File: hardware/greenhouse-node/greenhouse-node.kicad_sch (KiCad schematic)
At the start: 53 parts, among them J1 Conn_01x12_Male, J2 Conn_01x02_Male, J3 Conn_01x02_Male, J4 Conn_01x02_Male, J5 Conn_01x04_Male, J7 Conn_01x02_Male, Q1 BC549C, Q2 BC549C, Q3 IRF9530N, Q4 IRF530N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

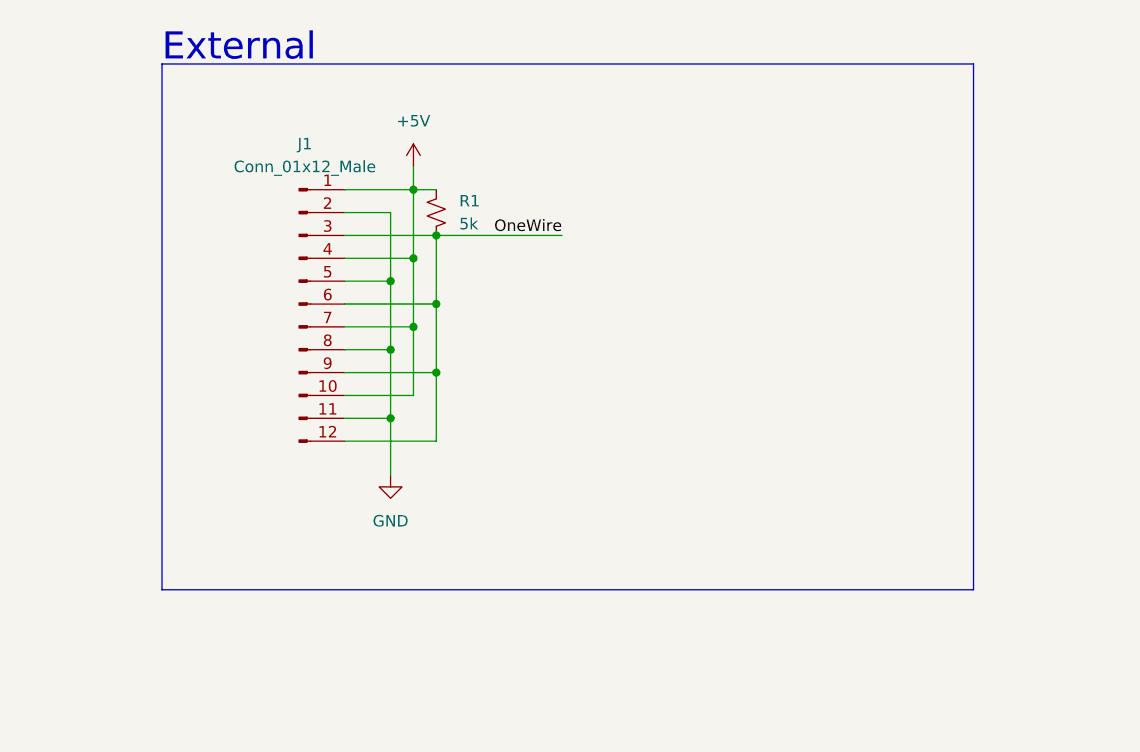
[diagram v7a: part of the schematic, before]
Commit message: Implement HC-12 on node
Also removed switch logic and old shift register
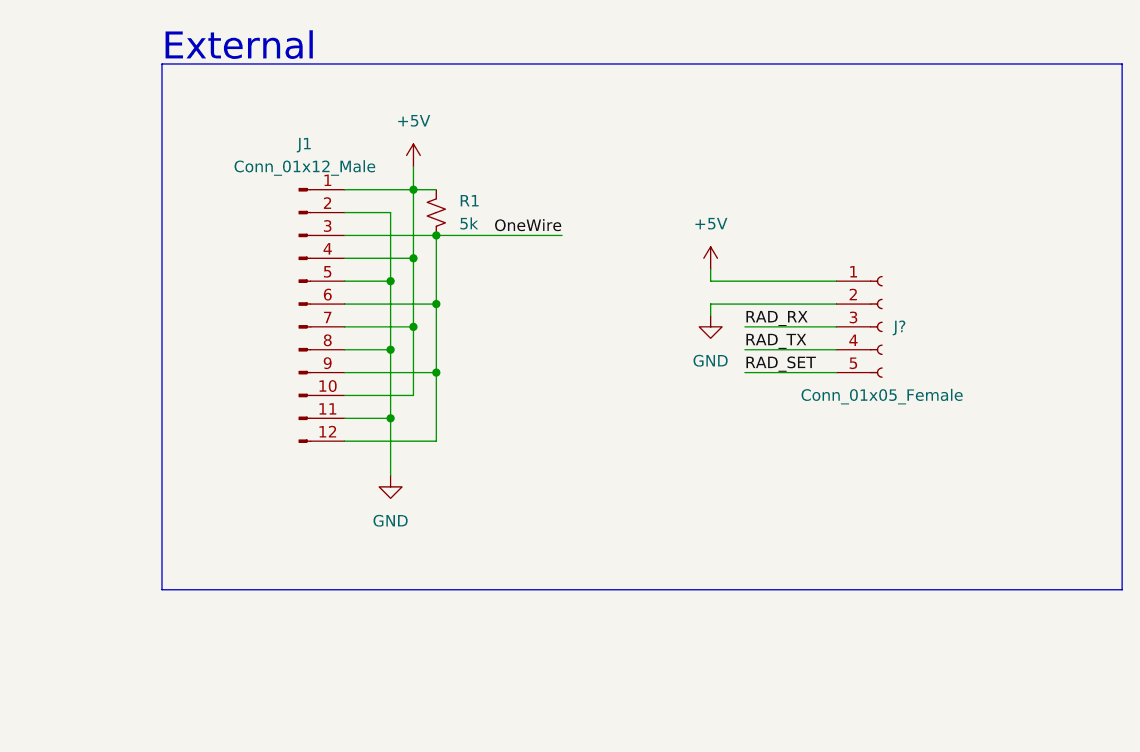
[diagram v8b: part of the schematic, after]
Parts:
- added J?: Conn_01x05_Female, Connector_PinSocket_2.54mm:PinSocket_1x05_P2.54mm_Vertical, symbol Connector:Conn_01x05_Female
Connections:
- net +5V: now also J?.1 (Pin_1)
- net GND: now also J?.2 (Pin_2)
- net RAD_RX: now also J?.3 (Pin_3)
- net RAD_TX: now also J?.4 (Pin_4)
- new net RAD_SET: J?.5 (Pin_5)
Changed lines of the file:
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@@
+    (stroke (width 0) (type default) (color 0 0 0 0))
+  )
+  (wire (pts (xy 281.94 64.77) (xy 292.1 64.77))
     (stroke (width 0) (type default) (color 0 0 0 0))
   )
@@
     (stroke (width 0) (type default) (color 0 0 0 0))
   )
+  (wire (pts (xy 278.13 58.42) (xy 278.13 59.69))
+    (stroke (width 0) (type default) (color 0 0 0 0))
+  )
   (wire (pts (xy 242.57 59.69) (xy 242.57 52.07))
     (stroke (width 0) (type default) (color 0 0 0 0))
@@
     (stroke (width 0) (type default) (color 0 0 0 0))
   )
+  (wire (pts (xy 281.94 69.85) (xy 292.1 69.85))
+    (stroke (width 0) (type default) (color 0 0 0 0))
+  )
   (wire (pts (xy 299.72 213.36) (xy 311.15 213.36))
     (stroke (width 0) (type default) (color 0 0 0 0))
@@
     (stroke (width 0) (type default) (color 0 0 0 0))
   )
+  (wire (pts (xy 278.13 62.23) (xy 278.13 63.5))
+    (stroke (width 0) (type default) (color 0 0 0 0))
+  )
+  (wire (pts (xy 281.94 67.31) (xy 292.1 67.31))
+    (stroke (width 0) (type default) (color 0 0 0 0))
+  )
   (wire (pts (xy 119.38 158.75) (xy 133.35 158.75))
     (stroke (width 0) (type default) (color 0 0 0 0))
@@
     (stroke (width 0) (type default) (color 0 0 0 0))
   )
+  (wire (pts (xy 278.13 59.69) (xy 292.1 59.69))
+    (stroke (width 0) (type default) (color 0 0 0 0))
+  )
   (wire (pts (xy 256.54 166.37) (xy 256.54 163.83))
     (stroke (width 0) (type default) (color 0 0 0 0))
@@
     (stroke (width 0) (type default) (color 0 0 0 0))
   )
-  (polyline (pts (xy 217.17 93.98) (xy 307.34 93.98))
+  (polyline (pts (xy 217.17 93.98) (xy 323.85 93.98))
     (stroke (width 0) (type default) (color 0 0 0 0))
   )
@@
     (stroke (width 0) (type default) (color 0 0 0 0))
   )
+  (wire (pts (xy 292.1 62.23) (xy 278.13 62.23))
+    (stroke (width 0) (type default) (color 0 0 0 0))
+  )
   (wire (pts (xy 149.86 78.74) (xy 152.4 78.74))
     (stroke (width 0) (type default) (color 0 0 0 0))
   )
-  (polyline (pts (xy 307.34 35.56) (xy 217.17 35.56))
+  (polyline (pts (xy 323.85 35.56) (xy 217.17 35.56))
     (stroke (width 0) (type default) (color 0 0 0 0))
   )
@@
     (stroke (width 0) (type default) (color 0 0 0 0))
   )
-  (polyline (pts (xy 307.34 93.98) (xy 307.34 35.56))
+  (polyline (pts (xy 323.85 93.98) (xy 323.85 35.56))
     (stroke (width 0) (type default) (color 0 0 0 0))
   )
@@
     (effects (font (size 1.27 1.27)) (justify right bottom))
   )
+  (label "RAD_TX" (at 281.94 67.31 0)
+    (effects (font (size 1.27 1.27)) (justify left bottom))
+  )
   (label "LED_G" (at 153.67 185.42 0)
     (effects (font (size 1.27 1.27)) (justify left bottom))
@@
     (effects (font (size 1.27 1.27)) (justify right bottom))
   )
+  (label "RAD_RX" (at 281.94 64.77 0)
+    (effects (font (size 1.27 1.27)) (justify left bottom))
+  )
   (label "LED_R" (at 153.67 195.58 0)
     (effects (font (size 1.27 1.27)) (justify left bottom))
@@
   (label "SR_CLK" (at 124.46 227.33 180)
     (effects (font (size 1.27 1.27)) (justify right bottom))
+  )
+  (label "RAD_SET" (at 281.94 69.85 0)
+    (effects (font (size 1.27 1.27)) (justify left bottom))
   )
   (label "XTAL2" (at 125.73 212.09 0)
@@
       (effects (font (size 1.27 1.27)) hide)
     )
+  )
+  (symbol (lib_id "Connector:Conn_01x05_Female") (at 297.18 64.77 0) (unit 1)
+    (in_bom yes) (on_board yes) (fields_autoplaced)
+    (property "Reference" "J?" (id 0) (at 298.45 64.7699 0)
+      (effects (font (size 1.27 1.27)) (justify left))
+    )
+    (property "Value" "Conn_01x05_Female" (id 1) (at 297.18 72.39 0))
+    (property "Footprint" "Connector_PinSocket_2.54mm:PinSocket_1x05_P2.54mm_Vertical" (id 2) (at 297.18 64.77 0)
+      (effects (font (size 1.27 1.27)) hide)
+    )
+    (property "Datasheet" "~" (id 3) (at 297.18 64.77 0)
+      (effects (font (size 1.27 1.27)) hide)
+    )
+    (pin "1")
+    (pin "2")
+    (pin "3")
+    (pin "4")
+    (pin "5")
   )
   (symbol (lib_id "power:GND") (at 293.37 184.15 0) (mirror y) (unit 1)
@@
     (pin "2")
   )
+  (symbol (lib_id "power:GND") (at 278.13 63.5 0) (unit 1)
+    (in_bom yes) (on_board yes) (fields_autoplaced)
+    (property "Reference" "#PWR?" (id 0) (at 278.13 69.85 0)
+      (effects (font (size 1.27 1.27)) hide)
+    )
+    (property "Value" "GND" (id 1) (at 278.13 68.58 0))
+    (property "Footprint" "" (id 2) (at 278.13 63.5 0)
+      (effects (font (size 1.27 1.27)) hide)
+    )
+    (property "Datasheet" "" (id 3) (at 278.13 63.5 0)
+      (effects (font (size 1.27 1.27)) hide)
+    )
+    (pin "1")
+  )
   (symbol (lib_id "power:GND") (at 138.43 80.01 0) (unit 1)
     (in_bom yes) (on_board yes) (fields_autoplaced)
@@
     (pin "1")
     (pin "2")
+  )
+  (symbol (lib_id "power:+5V") (at 278.13 58.42 0) (mirror y) (unit 1)
+    (in_bom yes) (on_board yes) (fields_autoplaced)
+    (property "Reference" "#PWR?" (id 0) (at 278.13 62.23 0)
+      (effects (font (size 1.27 1.27)) hide)
+    )
+    (property "Value" "+5V" (id 1) (at 278.13 53.34 0))
+    (property "Footprint" "" (id 2) (at 278.13 58.42 0)
+      (effects (font (size 1.27 1.27)) hide)
+    )
+    (property "Datasheet" "" (id 3) (at 278.13 58.42 0)
+      (effects (font (size 1.27 1.27)) hide)
+    )
+    (pin "1")
   )
   (symbol (lib_id "Device:C_Small") (at 90.17 135.89 270) (unit 1)
@@
       (reference "#PWR0110") (unit 1) (value "+12V") (footprint "")
     )
+    (path "/5490da7d-ed65-440d-ac44-76ef4a92730b"
+      (reference "#PWR?") (unit 1) (value "GND") (footprint "")
+    )
+    (path "/62a9d125-308e-4e87-85cc-8951bfc63530"
+      (reference "#PWR?") (unit 1) (value "+5V") (footprint "")
+    )
     (path "/695ccbcc-4a44-4a1f-b5e4-e7c0459755d8"
       (reference "C1") (unit 1) (value "100uF") (footprint "Capacitor_THT:C_Radial_D5.0mm_H7.0mm_P2.00mm")
@@
       (reference "J7") (unit 1) (value "Conn_01x02_Male") (footprint "Connector_Molex:Molex_KK-396_A-41791-0002_1x02_P3.96mm_Vertical")
     )
+    (path "/03526edb-5f75-4d50-986c-9ed8ba07008e"
+      (reference "J?") (unit 1) (value "Conn_01x05_Female") (footprint "Connector_PinSocket_2.54mm:PinSocket_1x05_P2.54mm_Vertical")
+    )
     (path "/12a683d0-a64c-4803-a34c-fe334bd2d471"
